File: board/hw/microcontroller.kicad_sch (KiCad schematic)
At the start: 20 parts, among them J1 SWD, U1 RP2040, U2 M24C02-FMN, U4 W25Q32JVSS, Y1 Crystal

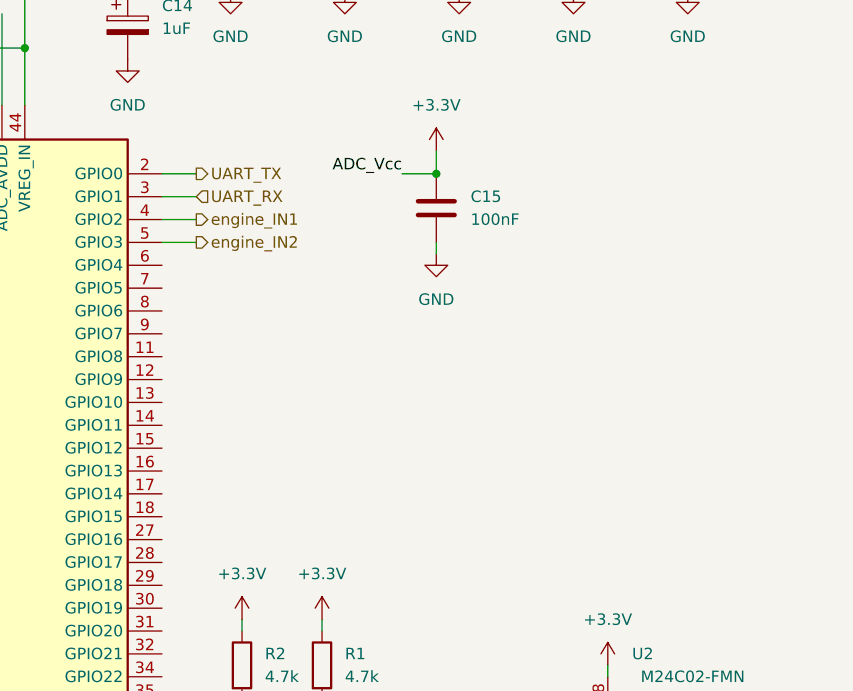
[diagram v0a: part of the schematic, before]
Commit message: added green LED, controllable from µC
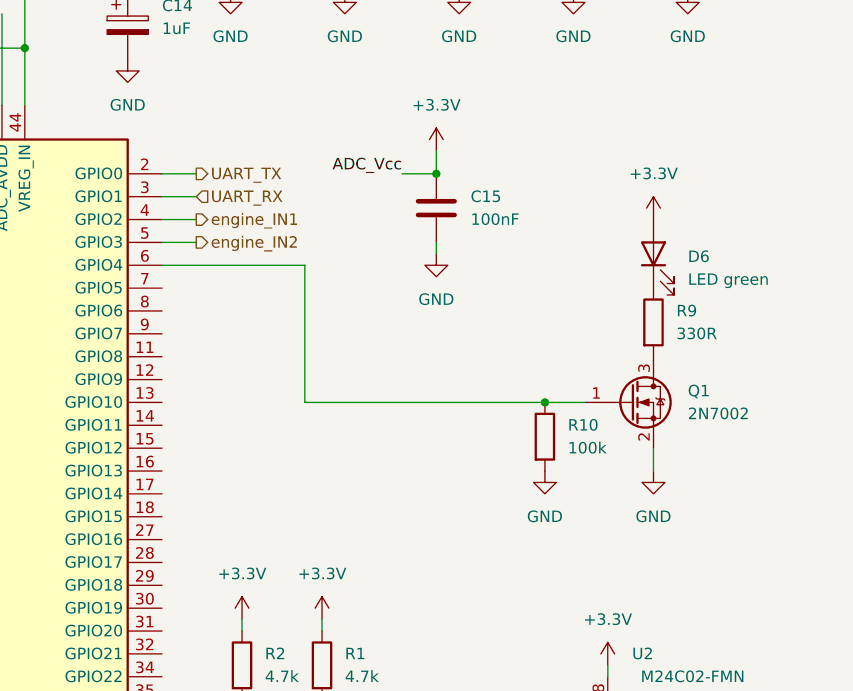
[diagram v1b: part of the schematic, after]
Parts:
- added D6: LED green, LED_SMD:LED_0805_2012Metric_Pad1.15x1.40mm_HandSolder, symbol Device:LED
- added Q1: 2N7002, Package_TO_SOT_SMD:SOT-23, symbol Transistor_FET:2N7002
- added R10: 100k, Resistor_SMD:R_0603_1608Metric, symbol Device:R
- added R9: 330R, Resistor_SMD:R_0805_2012Metric, symbol Device:R
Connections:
- net +3.3V: now also D6.2 (A)
- net GND: now also Q1.2 (S), R10.2
- net at U1.6 (GPIO4): now also Q1.1 (G), R10.1
- new net: Q1.3 (D), R9.2
- new net: D6.1 (K), R9.1
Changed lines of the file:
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@@
   (junction (at 194.31 27.94) (diameter 0) (color 0 0 0 0)
   )
+  (junction (at 216.535 81.28) (diameter 0) (color 0 0 0 0)
+  )
   (junction (at 204.47 55.88) (diameter 0) (color 0 0 0 0)
   )
@@
     (stroke (width 0) (type default))
   )
+  (wire (pts (xy 228.6 88.9) (xy 228.6 86.36))
+    (stroke (width 0) (type default))
+  )
   (wire (pts (xy 182.88 105.41) (xy 182.88 106.68))
     (stroke (width 0) (type default))
@@
     (stroke (width 0) (type default))
   )
+  (wire (pts (xy 189.865 81.28) (xy 216.535 81.28))
+    (stroke (width 0) (type default))
+  )
   (wire (pts (xy 153.67 41.91) (xy 158.75 41.91))
     (stroke (width 0) (type default))
@@
     (stroke (width 0) (type default))
   )
+  (wire (pts (xy 216.535 81.28) (xy 220.98 81.28))
+    (stroke (width 0) (type default))
+  )
   (wire (pts (xy 143.51 44.45) (xy 143.51 48.26))
     (stroke (width 0) (type default))
@@
     (stroke (width 0) (type default))
   )
+  (wire (pts (xy 189.865 66.04) (xy 189.865 81.28))
+    (stroke (width 0) (type default))
+  )
   (wire (pts (xy 125.73 36.83) (xy 143.51 36.83))
     (stroke (width 0) (type default))
@@
   )
   (wire (pts (xy 173.99 60.96) (xy 177.8 60.96))
+    (stroke (width 0) (type default))
+  )
+  (wire (pts (xy 173.99 66.04) (xy 189.865 66.04))
     (stroke (width 0) (type default))
   )
@@
   (hierarchical_label "engine_IN1" (shape output) (at 177.8 60.96 0) (fields_autoplaced)
     (effects (font (size 1.27 1.27)) (justify left))
+  )
+  (symbol (lib_id "Device:R") (at 216.535 85.09 0) (unit 1)
+    (in_bom yes) (on_board yes) (dnp no) (fields_autoplaced)
+    (property "Reference" "R10" (at 219.075 83.82 0)
+      (effects (font (size 1.27 1.27)) (justify left))
+    )
+    (property "Value" "100k" (at 219.075 86.36 0)
+      (effects (font (size 1.27 1.27)) (justify left))
+    )
+    (property "Footprint" "Resistor_SMD:R_0603_1608Metric" (at 214.757 85.09 90)
+      (effects (font (size 1.27 1.27)) hide)
+    )
+    (property "Datasheet" "~" (at 216.535 85.09 0)
+      (effects (font (size 1.27 1.27)) hide)
+    )
+    (pin "2")
+    (pin "1")
+    (instances
+      (project "yals"
+        (path "/920838ab-42d6-4f6a-a4ed-bf4606dd42d5/8ac632fc-8d3b-4983-8745-f2671c397aa7"
+          (reference "R10") (unit 1)
+        )
+      )
+    )
   )
   (symbol (lib_id "power:+3.3V") (at 204.47 53.34 0) (mirror y) (unit 1)
@@
     )
   )
+  (symbol (lib_id "Transistor_FET:2N7002") (at 226.06 81.28 0) (unit 1)
+    (in_bom yes) (on_board yes) (dnp no) (fields_autoplaced)
+    (property "Reference" "Q1" (at 232.41 80.01 0)
+      (effects (font (size 1.27 1.27)) (justify left))
+    )
+    (property "Value" "2N7002" (at 232.41 82.55 0)
+      (effects (font (size 1.27 1.27)) (justify left))
+    )
+    (property "Footprint" "Package_TO_SOT_SMD:SOT-23" (at 231.14 83.185 0)
+      (effects (font (size 1.27 1.27) italic) (justify left) hide)
+    )
+    (property "Datasheet" "https://www.onsemi.com/pub/Collateral/NDS7002A-D.PDF" (at 231.14 85.09 0)
+      (effects (font (size 1.27 1.27)) (justify left) hide)
+    )
+    (pin "3")
+    (pin "2")
+    (pin "1")
+    (instances
+      (project "yals"
+        (path "/920838ab-42d6-4f6a-a4ed-bf4606dd42d5/8ac632fc-8d3b-4983-8745-f2671c397aa7"
+          (reference "Q1") (unit 1)
+        )
+      )
+    )
+  )
+  (symbol (lib_id "Device:LED") (at 228.6 64.77 90) (unit 1)
+    (in_bom yes) (on_board yes) (dnp no) (fields_autoplaced)
+    (property "Reference" "D6" (at 232.41 65.0875 90)
+      (effects (font (size 1.27 1.27)) (justify right))
+    )
+    (property "Value" "LED green" (at 232.41 67.6275 90)
+      (effects (font (size 1.27 1.27)) (justify right))
+    )
+    (property "Footprint" "LED_SMD:LED_0805_2012Metric_Pad1.15x1.40mm_HandSolder" (at 228.6 64.77 0)
+      (effects (font (size 1.27 1.27)) hide)
+    )
+    (property "Datasheet" "~" (at 228.6 64.77 0)
+      (effects (font (size 1.27 1.27)) hide)
+    )
+    (pin "1")
+    (pin "2")
+    (instances
+      (project "yals"
+        (path "/920838ab-42d6-4f6a-a4ed-bf4606dd42d5/8ac632fc-8d3b-4983-8745-f2671c397aa7"
+          (reference "D6") (unit 1)
+        )
+      )
+    )
+  )
   (symbol (lib_id "Device:C_Polarized") (at 170.18 39.37 0) (unit 1)
     (in_bom yes) (on_board yes) (dnp no) (fields_autoplaced)
@@
         (path "/920838ab-42d6-4f6a-a4ed-bf4606dd42d5/8ac632fc-8d3b-4983-8745-f2671c397aa7"
           (reference "C14") (unit 1)
+        )
+      )
+    )
+  )
+  (symbol (lib_id "power:GND") (at 216.535 88.9 0) (unit 1)
+    (in_bom yes) (on_board yes) (dnp no) (fields_autoplaced)
+    (property "Reference" "#PWR054" (at 216.535 95.25 0)
+      (effects (font (size 1.27 1.27)) hide)
+    )
+    (property "Value" "GND" (at 216.535 93.98 0)
+      (effects (font (size 1.27 1.27)))
+    )
+    (property "Footprint" "" (at 216.535 88.9 0)
+      (effects (font (size 1.27 1.27)) hide)
+    )
+    (property "Datasheet" "" (at 216.535 88.9 0)
+      (effects (font (size 1.27 1.27)) hide)
+    )
+    (pin "1")
+    (instances
+      (project "yals"
+        (path "/920838ab-42d6-4f6a-a4ed-bf4606dd42d5/8ac632fc-8d3b-4983-8745-f2671c397aa7"
+          (reference "#PWR054") (unit 1)
         )
       )
@@
     )
   )
+  (symbol (lib_id "power:+3.3V") (at 228.6 60.96 0) (mirror y) (unit 1)
+    (in_bom yes) (on_board yes) (dnp no) (fields_autoplaced)
+    (property "Reference" "#PWR052" (at 228.6 64.77 0)
+      (effects (font (size 1.27 1.27)) hide)
+    )
+    (property "Value" "+3.3V" (at 228.6 55.88 0)
+      (effects (font (size 1.27 1.27)))
+    )
+    (property "Footprint" "" (at 228.6 60.96 0)
+      (effects (font (size 1.27 1.27)) hide)
+    )
+    (property "Datasheet" "" (at 228.6 60.96 0)
+      (effects (font (size 1.27 1.27)) hide)
+    )
+    (pin "1")
+    (instances
+      (project "yals"
+        (path "/920838ab-42d6-4f6a-a4ed-bf4606dd42d5/8ac632fc-8d3b-4983-8745-f2671c397aa7"
+          (reference "#PWR052") (unit 1)
+        )
+      )
+    )
+  )
   (symbol (lib_id "power:+3.3V") (at 173.99 27.94 0) (mirror y) (unit 1)
     (in_bom yes) (on_board yes) (dnp no) (fields_autoplaced)
@@
     )
   )
+  (symbol (lib_id "power:GND") (at 228.6 88.9 0) (unit 1)
+    (in_bom yes) (on_board yes) (dnp no) (fields_autoplaced)
+    (property "Reference" "#PWR053" (at 228.6 95.25 0)
+      (effects (font (size 1.27 1.27)) hide)
+    )
+    (property "Value" "GND" (at 228.6 93.98 0)
+      (effects (font (size 1.27 1.27)))
+    )
+    (property "Footprint" "" (at 228.6 88.9 0)
+      (effects (font (size 1.27 1.27)) hide)
+    )
+    (property "Datasheet" "" (at 228.6 88.9 0)
+      (effects (font (size 1.27 1.27)) hide)
+    )
+    (pin "1")
+    (instances
+      (project "yals"
+        (path "/920838ab-42d6-4f6a-a4ed-bf4606dd42d5/8ac632fc-8d3b-4983-8745-f2671c397aa7"
+          (reference "#PWR053") (unit 1)
+        )
+      )
+    )
+  )
   (symbol (lib_id "Jumper:Jumper_2_Open") (at 99.06 57.15 0) (unit 1)
     (in_bom yes) (on_board yes) (dnp no) (fields_autoplaced)
@@
         )
       )
+    )
+  )
+  (symbol (lib_id "Device:R") (at 228.6 72.39 0) (unit 1)
+    (in_bom yes) (on_board yes) (dnp no) (fields_autoplaced)
+    (property "Reference" "R9" (at 231.14 71.12 0)
+      (effects (font (size 1.27 1.27)) (justify left))
+    )
+    (property "Value" "330R" (at 231.14 73.66 0)
+      (effects (font (size 1.27 1.27)) (justify left))
+    )
+    (property "Footprint" "Resistor_SMD:R_0805_2012Metric" (at 226.822 72.39 90)
+      (effects (font (size 1.27 1.27)) hide)
+    )
+    (property "Datasheet" "~" (at 228.6 72.39 0)
+      (effects (font (size 1.27 1.27)) hide)
+    )
+    (pin "2")
+    (pin "1")
+    (instances
+      (project "yals"
+        (path "/920838ab-42d6-4f6a-a4ed-bf4606dd42d5/8ac632fc-8d3b-4983-8745-f2671c397aa7"
+          (reference "R9") (unit 1)
+        )
+      )

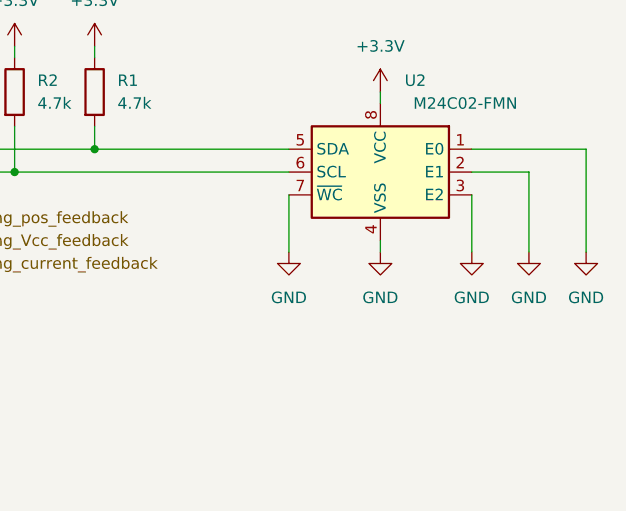
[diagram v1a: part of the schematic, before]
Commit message: ~WC pin of EEPROM chip is left floating, to make writes possible
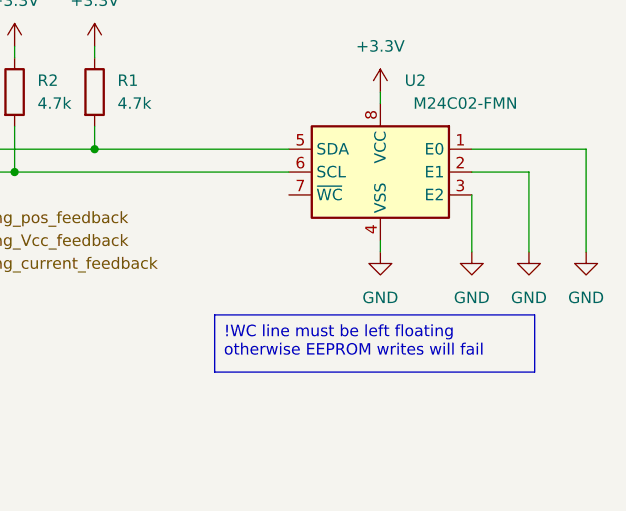
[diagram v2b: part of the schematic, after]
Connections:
- net GND: no longer U2.7 (~{WC})
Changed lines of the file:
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@@
-    (stroke (width 0) (type default))
-  )
-  (wire (pts (xy 213.36 128.27) (xy 213.36 121.92))
     (stroke (width 0) (type default))
   )
@@
   (wire (pts (xy 173.99 66.04) (xy 189.865 66.04))
     (stroke (width 0) (type default))
+  )
+  (text_box "!WC line must be left floating\notherwise EEPROM writes will fail"
+    (at 205.105 135.255 0) (size 35.56 6.35)
+    (stroke (width 0) (type default))
+    (fill (type none))
+    (effects (font (size 1.27 1.27)) (justify left top))
   )
   (label "pico_run" (at 120.65 55.88 180) (fields_autoplaced)
@@
         )
       )
-    )
-  )
-  (symbol (lib_id "power:GND") (at 213.36 128.27 0) (mirror y) (unit 1)
-    (in_bom yes) (on_board yes) (dnp no) (fields_autoplaced)
-    (property "Reference" "#PWR019" (at 213.36 134.62 0)
-      (effects (font (size 1.27 1.27)) hide)
-    )
-    (property "Value" "GND" (at 213.36 133.35 0)
-      (effects (font (size 1.27 1.27)))
-    )
-    (property "Footprint" "" (at 213.36 128.27 0)
-      (effects (font (size 1.27 1.27)) hide)
-    )
-    (property "Datasheet" "" (at 213.36 128.27 0)
-      (effects (font (size 1.27 1.27)) hide)
-    )
-    (pin "1")
-    (instances
-      (project "yals"
-        (path "/920838ab-42d6-4f6a-a4ed-bf4606dd42d5/8ac632fc-8d3b-4983-8745-f2671c397aa7"
-          (reference "#PWR019") (unit 1)
-        )
-      )
